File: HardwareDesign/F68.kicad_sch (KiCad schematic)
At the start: 2 parts, among them J001 Conn_02x40_Odd_Even

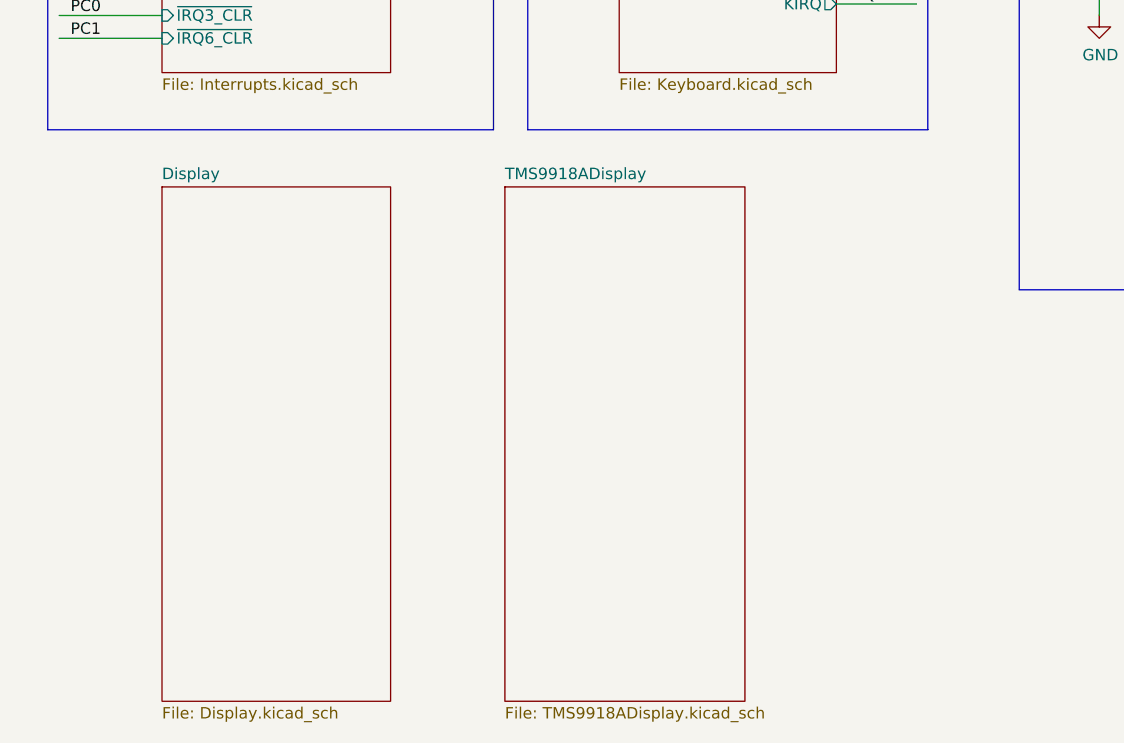
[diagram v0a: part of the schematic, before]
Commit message: prepare to create PCB for TMS9918A module
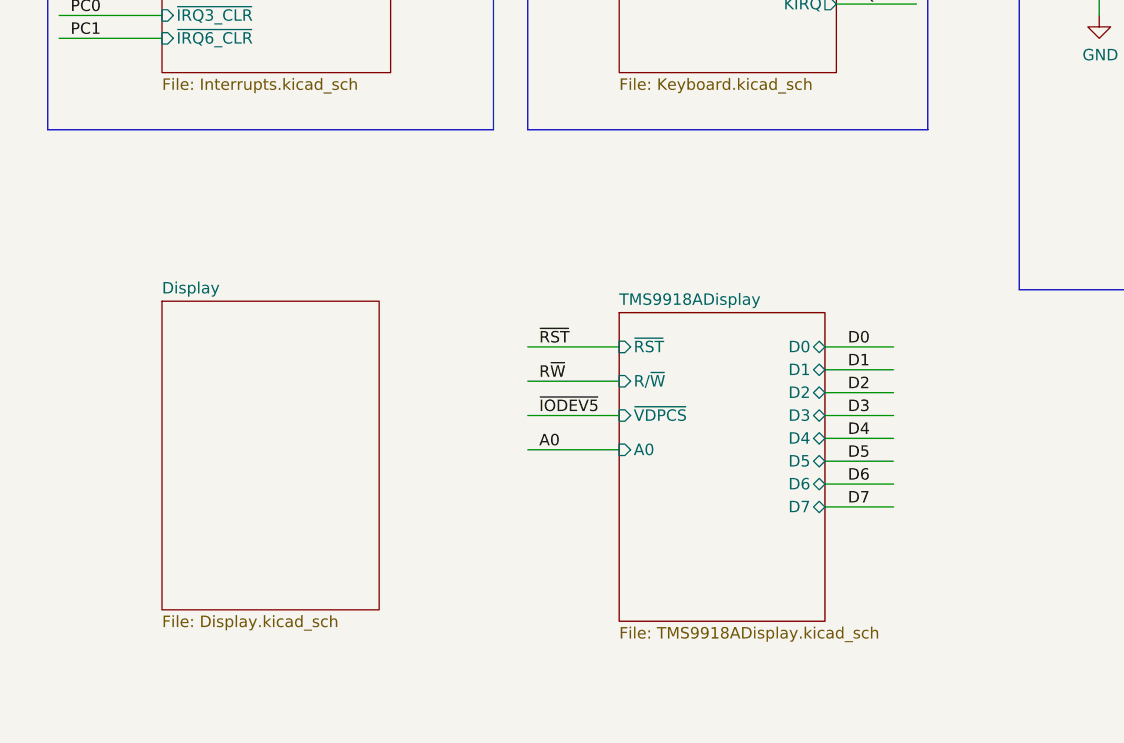
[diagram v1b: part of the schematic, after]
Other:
- sheet TMS9918ADisplay ports: added A0, D0, D1, D2, D3, D4, D5, D6, D7, R/~{W}, ~{RST}, ~{VDPCS}; removed none

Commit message: add support for VDP interrupt
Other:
- sheet TMS9918ADisplay ports: added ~{VDPINT}; removed none
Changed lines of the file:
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@@
+    (stroke (width 0) (type default) (color 0 0 0 0))
+  )
+  (wire (pts (xy 195.58 220.98) (xy 203.2 220.98))
     (stroke (width 0) (type default) (color 0 0 0 0))
   )
@@
   )
   (label "A9" (at 120.65 81.28 0)
+    (effects (font (size 1.27 1.27)) (justify left bottom))
+  )
+  (label "~{IRQ2}" (at 196.85 220.98 0)
     (effects (font (size 1.27 1.27)) (justify left bottom))
   )
@@
       (effects (font (size 1.27 1.27)) (justify right))
     )
+    (pin "~{VDPINT}" output (at 195.58 220.98 0)
+      (effects (font (size 1.27 1.27)) (justify right))
+    )
   )
   (sheet_instances
@@
       (reference "J701") (unit 1) (value "RCJ-044") (footprint "CUI_RCJ-044:CUI_RCJ-044")
     )
+    (path "/d3704385-6c80-4c06-a060-a58a9dd421b5/231558bc-7ecb-46bf-95c0-8a93f50742c4"
+      (reference "J702") (unit 1) (value "Conn_01x02") (footprint "")
+    )
     (path "/d3704385-6c80-4c06-a060-a58a9dd421b5/330d5956-7999-4236-90df-a660f38e22eb"

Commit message: start working on YM2149 sound module
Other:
- added sheet YM2149_Sound (YM2149_Sound.kicad_sch)
- moved on the sheet: C001, J001

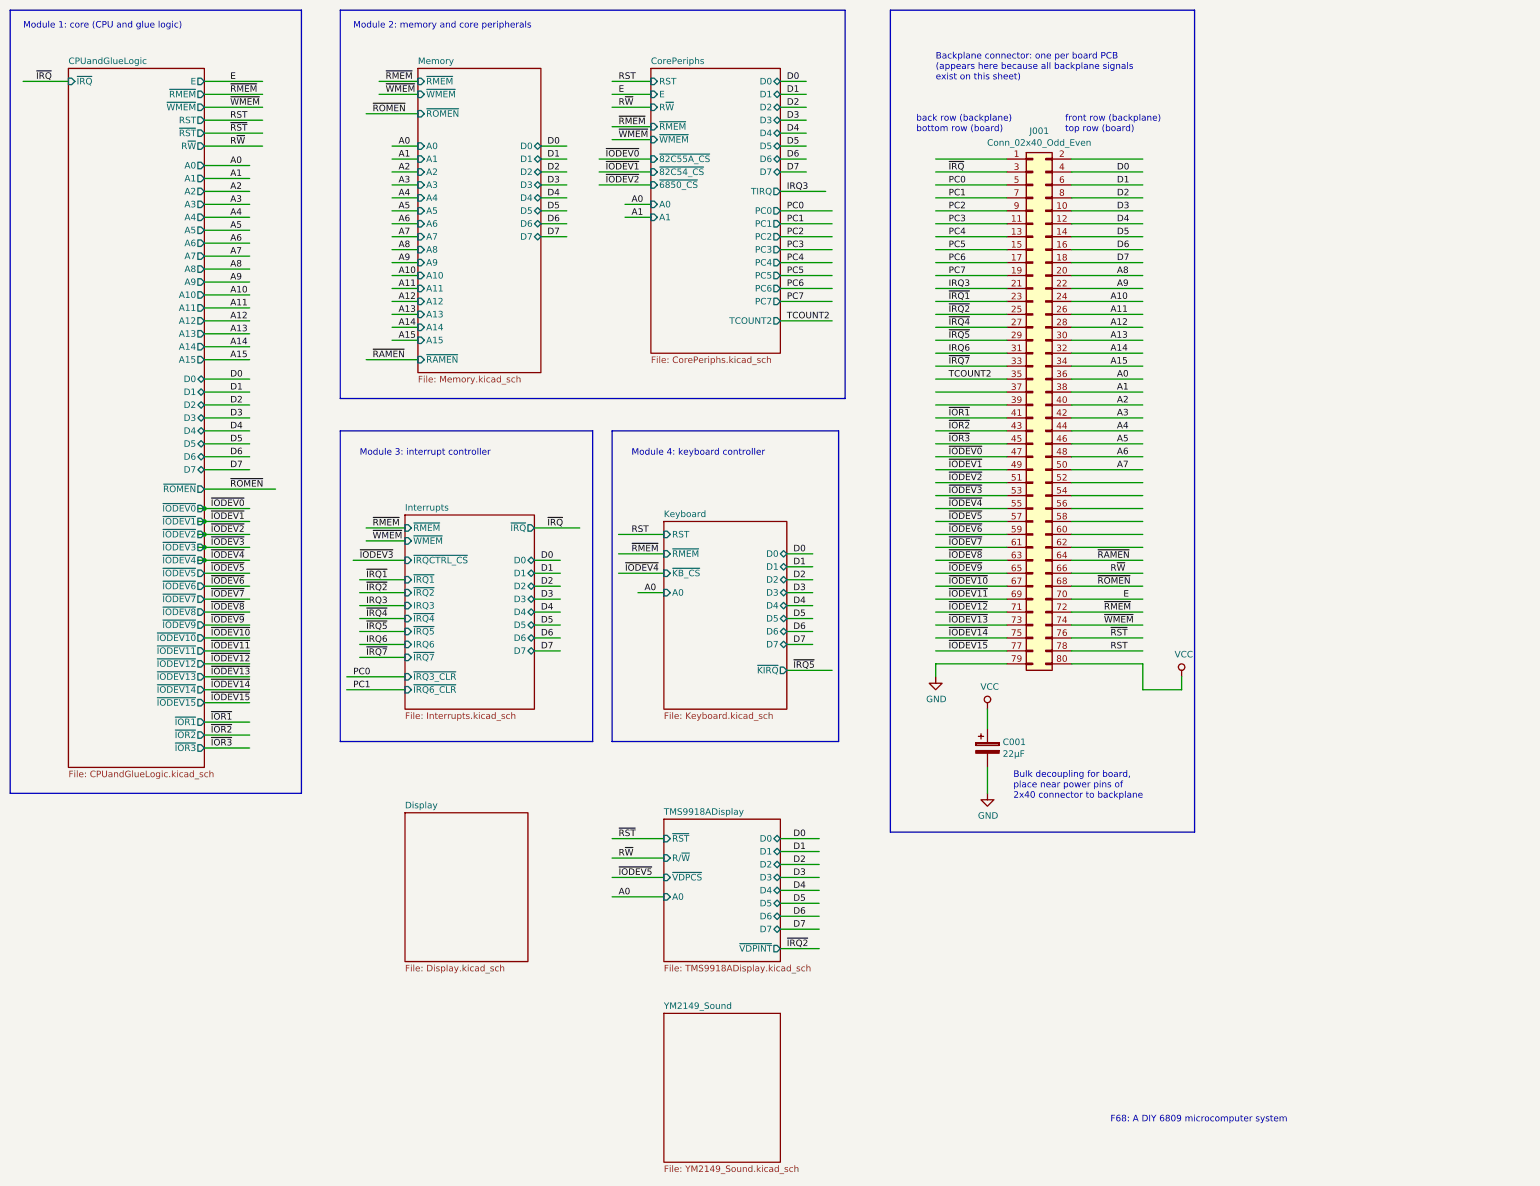
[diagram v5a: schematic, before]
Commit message: more work on YM2149 module
Also, rearranged top-level schematic a bit.
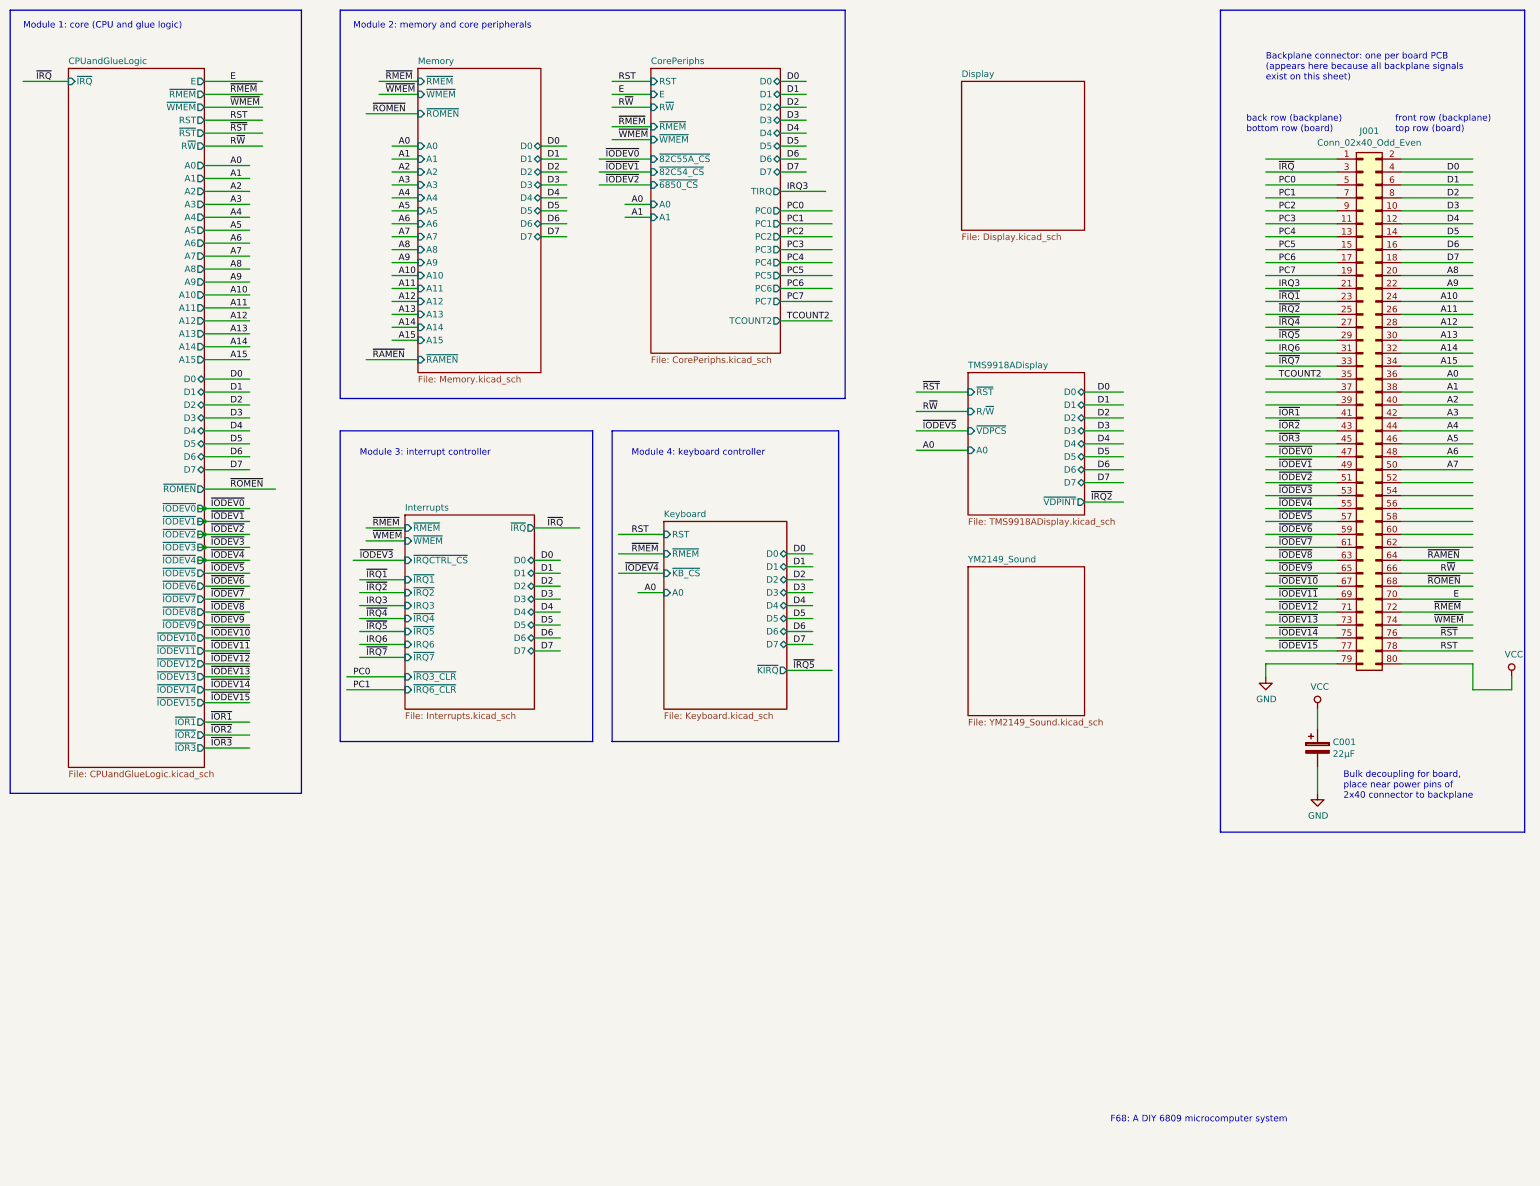
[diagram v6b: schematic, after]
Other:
- moved on the sheet: C001, J001
